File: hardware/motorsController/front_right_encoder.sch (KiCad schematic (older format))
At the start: 6 parts, among them Q1 Q_Photo_NPN

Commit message: add a pull-up to encoder's output
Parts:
- added R37: 1k, Resistor_SMD:R_0805_2012Metric, symbol Device:R_Small
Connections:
- net +3V3: now also R37.1
- net at Q1.1 (C), R29.2: now also R37.2
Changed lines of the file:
@@
 $Descr A4 11693 8268
 encoding utf-8
-Sheet 8 9
+Sheet 9 9
 Title ""
 Date ""
@@
 AR Path="/5FC04BEE/5FB0A7B2" Ref="D3"  Part="1"
 AR Path="/5FC04BF2/5FB0A7B2" Ref="D4"  Part="1"
-F 0 "D3" V 1739 2232 50  0000 R CNN
+F 0 "D4" V 1739 2232 50  0000 R CNN
 F 1 "LED" V 1648 2232 50  0000 R CNN
 F 2 "Connector_PinSocket_2.54mm:PinSocket_1x02_P2.54mm_Vertical" H 1700 2350 50  0001 C CNN
@@
 AR Path="/5FC04BEE/5FB0A7B8" Ref="Q3"  Part="1"
 AR Path="/5FC04BF2/5FB0A7B8" Ref="Q4"  Part="1"
-F 0 "Q3" H 2550 2300 50  0000 R CNN
+F 0 "Q4" H 2550 2300 50  0000 R CNN
 F 1 "Q_Photo_NPN" H 2950 2400 50  0000 R CNN
 F 2 "Connector_PinSocket_2.54mm:PinSocket_1x02_P2.54mm_Vertical" H 2450 2450 50  0001 C CNN
@@
 AR Path="/5FC04BEE/5FB0A7BE" Ref="#PWR0134"  Part="1"
 AR Path="/5FC04BF2/5FB0A7BE" Ref="#PWR0139"  Part="1"
-F 0 "#PWR0134" H 1700 2300 50  0001 C CNN
+F 0 "#PWR0139" H 1700 2300 50  0001 C CNN
 F 1 "GND" H 1705 2377 50  0000 C CNN
 F 2 "" H 1700 2550 50  0001 C CNN
@@
 AR Path="/5FC04BEE/5FB0A7C5" Ref="#PWR0135"  Part="1"
 AR Path="/5FC04BF2/5FB0A7C5" Ref="#PWR0140"  Part="1"
-F 0 "#PWR0135" H 1700 2000 50  0001 C CNN
+F 0 "#PWR0140" H 1700 2000 50  0001 C CNN
 F 1 "+3V3" H 1715 2323 50  0000 C CNN
 F 2 "" H 1700 2150 50  0001 C CNN
@@
 AR Path="/5FC04BEE/5FB0A7CC" Ref="#PWR0136"  Part="1"
 AR Path="/5FC04BF2/5FB0A7CC" Ref="#PWR0141"  Part="1"
-F 0 "#PWR0136" H 2350 2350 50  0001 C CNN
+F 0 "#PWR0141" H 2350 2350 50  0001 C CNN
 F 1 "GND" H 2355 2427 50  0000 C CNN
 F 2 "" H 2350 2600 50  0001 C CNN
@@
 AR Path="/5FC04BEE/5FB0A7D3" Ref="C9"  Part="1"
 AR Path="/5FC04BF2/5FB0A7D3" Ref="C11"  Part="1"
-F 0 "C9" H 3592 2296 50  0000 L CNN
+F 0 "C11" H 3592 2296 50  0000 L CNN
 F 1 "300pF" H 3592 2205 50  0000 L CNN
 F 2 "Capacitor_SMD:C_0805_2012Metric" H 3500 2250 50  0001 C CNN
@@
 AR Path="/5FC04BEE/5FB0A7D9" Ref="R33"  Part="1"
 AR Path="/5FC04BF2/5FB0A7D9" Ref="R35"  Part="1"
-F 0 "R33" V 3054 2100 50  0000 C CNN
+F 0 "R35" V 3054 2100 50  0000 C CNN
 F 1 "2M" V 3145 2100 50  0000 C CNN
 F 2 "Resistor_SMD:R_0805_2012Metric" H 3250 2100 50  0001 C CNN
@@
 AR Path="/5FC04BEE/5FB0B2E6" Ref="#PWR0137"  Part="1"
 AR Path="/5FC04BF2/5FB0B2E6" Ref="#PWR0142"  Part="1"
-F 0 "#PWR0137" H 3500 2150 50  0001 C CNN
+F 0 "#PWR0142" H 3500 2150 50  0001 C CNN
 F 1 "GND" H 3505 2227 50  0000 C CNN
 F 2 "" H 3500 2400 50  0001 C CNN
@@
 Wire Wire Line
 	2350 2150 2350 2100
-Wire Wire Line
-	2350 2100 3150 2100
 $Comp
 L Device:C_Small C6
@@
 AR Path="/5FC04BEE/5FB0F088" Ref="C10"  Part="1"
 AR Path="/5FC04BF2/5FB0F088" Ref="C12"  Part="1"
-F 0 "C10" V 3521 2100 50  0000 C CNN
+F 0 "C12" V 3521 2100 50  0000 C CNN
 F 1 "82nF" V 3612 2100 50  0000 C CNN
 F 2 "Capacitor_SMD:C_1206_3216Metric" H 3750 2100 50  0001 C CNN
@@
 AR Path="/5FC04BEE/5FB110C4" Ref="R34"  Part="1"
 AR Path="/5FC04BF2/5FB110C4" Ref="R36"  Part="1"
-F 0 "R34" H 4059 2296 50  0000 L CNN
+F 0 "R36" H 4059 2296 50  0000 L CNN
 F 1 "2M" H 4059 2205 50  0000 L CNN
 F 2 "Resistor_SMD:R_0805_2012Metric" H 4000 2250 50  0001 C CNN
@@
 AR Path="/5FC04BEE/5FB12EE4" Ref="#PWR0138"  Part="1"
 AR Path="/5FC04BF2/5FB12EE4" Ref="#PWR0143"  Part="1"
-F 0 "#PWR0138" H 4000 2150 50  0001 C CNN
+F 0 "#PWR0143" H 4000 2150 50  0001 C CNN
 F 1 "GND" H 4005 2227 50  0000 C CNN
 F 2 "" H 4000 2400 50  0001 C CNN
@@
 Wire Wire Line
 	4000 2400 4000 2350
+$Comp
+L power:+3.3V #PWR0144
+U 1 1 5FC0B227
+P 2950 1800
+AR Path="/5FB03879/5FC0B227" Ref="#PWR0144"  Part="1"
+AR Path="/5FBFC472/5FC0B227" Ref="#PWR0145"  Part="1"
+AR Path="/5FC04BEE/5FC0B227" Ref="#PWR0146"  Part="1"
+AR Path="/5FC04BF2/5FC0B227" Ref="#PWR0147"  Part="1"
+F 0 "#PWR0147" H 2950 1650 50  0001 C CNN
+F 1 "+3.3V" H 2965 1973 50  0000 C CNN
+F 2 "" H 2950 1800 50  0001 C CNN
+F 3 "" H 2950 1800 50  0001 C CNN
+	1    2950 1800
+	1    0    0    -1
+$EndComp
+$Comp
+L Device:R_Small R37
+U 1 1 5FC0D744
+P 2950 1950
+AR Path="/5FB03879/5FC0D744" Ref="R37"  Part="1"
+AR Path="/5FBFC472/5FC0D744" Ref="R38"  Part="1"
+AR Path="/5FC04BEE/5FC0D744" Ref="R39"  Part="1"
+AR Path="/5FC04BF2/5FC0D744" Ref="R40"  Part="1"
+F 0 "R40" H 3009 1996 50  0000 L CNN
+F 1 "1k" H 3009 1905 50  0000 L CNN
+F 2 "Resistor_SMD:R_0805_2012Metric" H 2950 1950 50  0001 C CNN
+F 3 "~" H 2950 1950 50  0001 C CNN
+	1    2950 1950
+	1    0    0    -1
+$EndComp
+Wire Wire Line
+	2950 1800 2950 1850
+Wire Wire Line
+	2950 2050 2950 2100
+Connection ~ 2950 2100
+Wire Wire Line
+	2950 2100 3150 2100
+Wire Wire Line
+	2350 2100 2950 2100
 $EndSCHEMATC

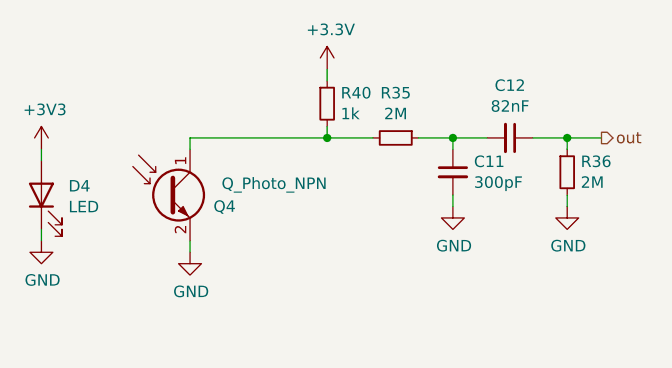
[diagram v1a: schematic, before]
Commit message: remove RC filter from collector and add resisor  before emiter
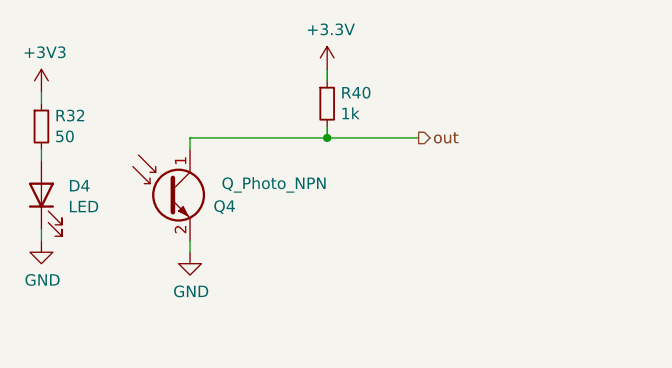
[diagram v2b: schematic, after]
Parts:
- removed C5: 300pF, Capacitor_SMD:C_0805_2012Metric, symbol Device:C_Small
- removed C6: 82nF, Capacitor_SMD:C_1206_3216Metric, symbol Device:C_Small
- removed R29, R30: 2M, Resistor_SMD:R_0805_2012Metric, symbol Device:R_Small
- added R31: 50, symbol Device:R_Small
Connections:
- net +3V3: now also R31.1; no longer D1.2 (A)
- net out: now also Q1.1 (C), R37.2
- new net: D1.2 (A), R31.2
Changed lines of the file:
@@
 $Descr A4 11693 8268
 encoding utf-8
-Sheet 9 9
+Sheet 8 9
 Title ""
 Date ""
@@
 L power:+3V3 #PWR0124
 U 1 1 5FB0A7C5
-P 1700 2150
+P 1700 1900
 AR Path="/5FB03879/5FB0A7C5" Ref="#PWR0124"  Part="1"
 AR Path="/5FBFC472/5FB0A7C5" Ref="#PWR0130"  Part="1"
 AR Path="/5FC04BEE/5FB0A7C5" Ref="#PWR0135"  Part="1"
 AR Path="/5FC04BF2/5FB0A7C5" Ref="#PWR0140"  Part="1"
-F 0 "#PWR0140" H 1700 2000 50  0001 C CNN
-F 1 "+3V3" H 1715 2323 50  0000 C CNN
-F 2 "" H 1700 2150 50  0001 C CNN
-F 3 "" H 1700 2150 50  0001 C CNN
-	1    1700 2150
+F 0 "#PWR0140" H 1700 1750 50  0001 C CNN
+F 1 "+3V3" H 1715 2073 50  0000 C CNN
+F 2 "" H 1700 1900 50  0001 C CNN
+F 3 "" H 1700 1900 50  0001 C CNN
+	1    1700 1900
 	1    0    0    -1
 $EndComp
@@
 Wire Wire Line
 	2350 2600 2350 2550
-$Comp
-L Device:C_Small C?
-U 1 1 5FB0A7D3
-P 3500 2250
-AR Path="/5FB0A7D3" Ref="C?"  Part="1"
-AR Path="/5FB03879/5FB0A7D3" Ref="C5"  Part="1"
-AR Path="/5FBFC472/5FB0A7D3" Ref="C7"  Part="1"
-AR Path="/5FC04BEE/5FB0A7D3" Ref="C9"  Part="1"
-AR Path="/5FC04BF2/5FB0A7D3" Ref="C11"  Part="1"
-F 0 "C11" H 3592 2296 50  0000 L CNN
-F 1 "300pF" H 3592 2205 50  0000 L CNN
-F 2 "Capacitor_SMD:C_0805_2012Metric" H 3500 2250 50  0001 C CNN
-F 3 "~" H 3500 2250 50  0001 C CNN
-	1    3500 2250
-	1    0    0    -1
-$EndComp
-$Comp
-L Device:R_Small R?
-U 1 1 5FB0A7D9
-P 3250 2100
-AR Path="/5FB0A7D9" Ref="R?"  Part="1"
-AR Path="/5FB03879/5FB0A7D9" Ref="R29"  Part="1"
-AR Path="/5FBFC472/5FB0A7D9" Ref="R31"  Part="1"
-AR Path="/5FC04BEE/5FB0A7D9" Ref="R33"  Part="1"
-AR Path="/5FC04BF2/5FB0A7D9" Ref="R35"  Part="1"
-F 0 "R35" V 3054 2100 50  0000 C CNN
-F 1 "2M" V 3145 2100 50  0000 C CNN
-F 2 "Resistor_SMD:R_0805_2012Metric" H 3250 2100 50  0001 C CNN
-F 3 "~" H 3250 2100 50  0001 C CNN
-	1    3250 2100
-	0    1    1    0
-$EndComp
-Wire Wire Line
-	3350 2100 3500 2100
-Wire Wire Line
-	3500 2100 3500 2150
-$Comp
-L power:GND #PWR0126
-U 1 1 5FB0B2E6
-P 3500 2400
-AR Path="/5FB03879/5FB0B2E6" Ref="#PWR0126"  Part="1"
-AR Path="/5FBFC472/5FB0B2E6" Ref="#PWR0132"  Part="1"
-AR Path="/5FC04BEE/5FB0B2E6" Ref="#PWR0137"  Part="1"
-AR Path="/5FC04BF2/5FB0B2E6" Ref="#PWR0142"  Part="1"
-F 0 "#PWR0142" H 3500 2150 50  0001 C CNN
-F 1 "GND" H 3505 2227 50  0000 C CNN
-F 2 "" H 3500 2400 50  0001 C CNN
-F 3 "" H 3500 2400 50  0001 C CNN
-	1    3500 2400
-	1    0    0    -1
-$EndComp
-Wire Wire Line
-	3500 2400 3500 2350
-Text HLabel 4150 2100 2    50   Output ~ 0
+Text HLabel 3350 2100 2    50   Output ~ 0
 out
 Wire Wire Line
 	2350 2150 2350 2100
-$Comp
-L Device:C_Small C6
-U 1 1 5FB0F088
-P 3750 2100
-AR Path="/5FB03879/5FB0F088" Ref="C6"  Part="1"
-AR Path="/5FBFC472/5FB0F088" Ref="C8"  Part="1"
-AR Path="/5FC04BEE/5FB0F088" Ref="C10"  Part="1"
-AR Path="/5FC04BF2/5FB0F088" Ref="C12"  Part="1"
-F 0 "C12" V 3521 2100 50  0000 C CNN
-F 1 "82nF" V 3612 2100 50  0000 C CNN
-F 2 "Capacitor_SMD:C_1206_3216Metric" H 3750 2100 50  0001 C CNN
-F 3 "~" H 3750 2100 50  0001 C CNN
-	1    3750 2100
-	0    1    1    0
-$EndComp
-Wire Wire Line
-	3650 2100 3500 2100
-Connection ~ 3500 2100
-$Comp
-L Device:R_Small R30
-U 1 1 5FB110C4
-P 4000 2250
-AR Path="/5FB03879/5FB110C4" Ref="R30"  Part="1"
-AR Path="/5FBFC472/5FB110C4" Ref="R32"  Part="1"
-AR Path="/5FC04BEE/5FB110C4" Ref="R34"  Part="1"
-AR Path="/5FC04BF2/5FB110C4" Ref="R36"  Part="1"
-F 0 "R36" H 4059 2296 50  0000 L CNN
-F 1 "2M" H 4059 2205 50  0000 L CNN
-F 2 "Resistor_SMD:R_0805_2012Metric" H 4000 2250 50  0001 C CNN
-F 3 "~" H 4000 2250 50  0001 C CNN
-	1    4000 2250
-	1    0    0    -1
-$EndComp
-Wire Wire Line
-	4000 2150 4000 2100
-Wire Wire Line
-	4000 2100 3850 2100
-Wire Wire Line
-	4150 2100 4000 2100
-Connection ~ 4000 2100
-$Comp
-L power:GND #PWR0127
-U 1 1 5FB12EE4
-P 4000 2400
-AR Path="/5FB03879/5FB12EE4" Ref="#PWR0127"  Part="1"
-AR Path="/5FBFC472/5FB12EE4" Ref="#PWR0133"  Part="1"
-AR Path="/5FC04BEE/5FB12EE4" Ref="#PWR0138"  Part="1"
-AR Path="/5FC04BF2/5FB12EE4" Ref="#PWR0143"  Part="1"
-F 0 "#PWR0143" H 4000 2150 50  0001 C CNN
-F 1 "GND" H 4005 2227 50  0000 C CNN
-F 2 "" H 4000 2400 50  0001 C CNN
-F 3 "" H 4000 2400 50  0001 C CNN
-	1    4000 2400
-	1    0    0    -1
-$EndComp
-Wire Wire Line
-	4000 2400 4000 2350
 $Comp
 L power:+3.3V #PWR0144
@@
 Connection ~ 2950 2100
 Wire Wire Line
-	2950 2100 3150 2100
+	2350 2100 2950 2100
 Wire Wire Line
-	2350 2100 2950 2100
+	2950 2100 3350 2100
+$Comp
+L Device:R_Small R31
+U 1 1 602F07E8
+P 1700 2050
+AR Path="/5FC04BEE/602F07E8" Ref="R31"  Part="1"
+AR Path="/5FBFC472/602F07E8" Ref="R30"  Part="1"
+AR Path="/5FB03879/602F07E8" Ref="R29"  Part="1"
+AR Path="/5FC04BF2/602F07E8" Ref="R32"  Part="1"
+F 0 "R32" H 1759 2096 50  0000 L CNN
+F 1 "50" H 1759 2005 50  0000 L CNN
+F 2 "" H 1700 2050 50  0001 C CNN
+F 3 "~" H 1700 2050 50  0001 C CNN
+	1    1700 2050
+	1    0    0    -1
+$EndComp
+Wire Wire Line
+	1700 1950 1700 1900
 $EndSCHEMATC

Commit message: layout a pcb for testing a motor driver
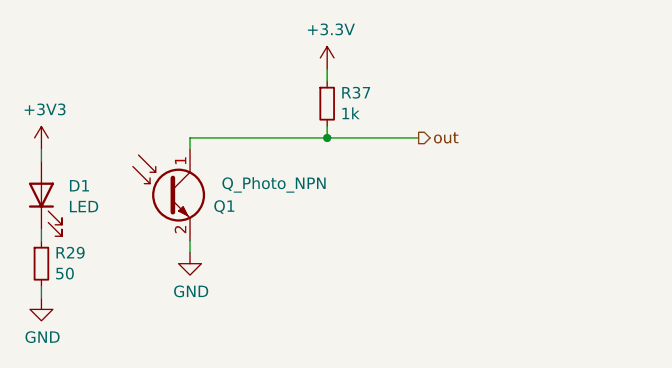
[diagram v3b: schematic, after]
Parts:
- R31: footprint (none) -> Resistor_SMD:R_0805_2012Metric
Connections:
- net +3V3: now also D1.2 (A); no longer R31.1
- net GND: now also R31.2; no longer D1.1 (K)
- new net: D1.1 (K), R31.1
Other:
- moved on the sheet: R29
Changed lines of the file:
@@
 $Descr A4 11693 8268
 encoding utf-8
-Sheet 8 9
+Sheet 6 9
 Title ""
 Date ""
@@
 AR Path="/5FC04BEE/5FB0A7B2" Ref="D3"  Part="1"
 AR Path="/5FC04BF2/5FB0A7B2" Ref="D4"  Part="1"
-F 0 "D4" V 1739 2232 50  0000 R CNN
+F 0 "D1" V 1739 2232 50  0000 R CNN
 F 1 "LED" V 1648 2232 50  0000 R CNN
 F 2 "Connector_PinSocket_2.54mm:PinSocket_1x02_P2.54mm_Vertical" H 1700 2350 50  0001 C CNN
@@
 AR Path="/5FC04BEE/5FB0A7B8" Ref="Q3"  Part="1"
 AR Path="/5FC04BF2/5FB0A7B8" Ref="Q4"  Part="1"
-F 0 "Q4" H 2550 2300 50  0000 R CNN
+F 0 "Q1" H 2550 2300 50  0000 R CNN
 F 1 "Q_Photo_NPN" H 2950 2400 50  0000 R CNN
 F 2 "Connector_PinSocket_2.54mm:PinSocket_1x02_P2.54mm_Vertical" H 2450 2450 50  0001 C CNN
@@
 L power:GND #PWR0123
 U 1 1 5FB0A7BE
-P 1700 2550
+P 1700 2800
 AR Path="/5FB03879/5FB0A7BE" Ref="#PWR0123"  Part="1"
 AR Path="/5FBFC472/5FB0A7BE" Ref="#PWR0129"  Part="1"
 AR Path="/5FC04BEE/5FB0A7BE" Ref="#PWR0134"  Part="1"
 AR Path="/5FC04BF2/5FB0A7BE" Ref="#PWR0139"  Part="1"
-F 0 "#PWR0139" H 1700 2300 50  0001 C CNN
-F 1 "GND" H 1705 2377 50  0000 C CNN
-F 2 "" H 1700 2550 50  0001 C CNN
-F 3 "" H 1700 2550 50  0001 C CNN
-	1    1700 2550
+F 0 "#PWR0123" H 1700 2550 50  0001 C CNN
+F 1 "GND" H 1705 2627 50  0000 C CNN
+F 2 "" H 1700 2800 50  0001 C CNN
+F 3 "" H 1700 2800 50  0001 C CNN
+	1    1700 2800
 	1    0    0    -1
 $EndComp
@@
 L power:+3V3 #PWR0124
 U 1 1 5FB0A7C5
-P 1700 1900
+P 1700 2150
 AR Path="/5FB03879/5FB0A7C5" Ref="#PWR0124"  Part="1"
 AR Path="/5FBFC472/5FB0A7C5" Ref="#PWR0130"  Part="1"
 AR Path="/5FC04BEE/5FB0A7C5" Ref="#PWR0135"  Part="1"
 AR Path="/5FC04BF2/5FB0A7C5" Ref="#PWR0140"  Part="1"
-F 0 "#PWR0140" H 1700 1750 50  0001 C CNN
-F 1 "+3V3" H 1715 2073 50  0000 C CNN
-F 2 "" H 1700 1900 50  0001 C CNN
-F 3 "" H 1700 1900 50  0001 C CNN
-	1    1700 1900
+F 0 "#PWR0124" H 1700 2000 50  0001 C CNN
+F 1 "+3V3" H 1715 2323 50  0000 C CNN
+F 2 "" H 1700 2150 50  0001 C CNN
+F 3 "" H 1700 2150 50  0001 C CNN
+	1    1700 2150
 	1    0    0    -1
 $EndComp
@@
 AR Path="/5FC04BEE/5FB0A7CC" Ref="#PWR0136"  Part="1"
 AR Path="/5FC04BF2/5FB0A7CC" Ref="#PWR0141"  Part="1"
-F 0 "#PWR0141" H 2350 2350 50  0001 C CNN
+F 0 "#PWR0125" H 2350 2350 50  0001 C CNN
 F 1 "GND" H 2355 2427 50  0000 C CNN
 F 2 "" H 2350 2600 50  0001 C CNN
@@
 AR Path="/5FC04BEE/5FC0B227" Ref="#PWR0146"  Part="1"
 AR Path="/5FC04BF2/5FC0B227" Ref="#PWR0147"  Part="1"
-F 0 "#PWR0147" H 2950 1650 50  0001 C CNN
+F 0 "#PWR0144" H 2950 1650 50  0001 C CNN
 F 1 "+3.3V" H 2965 1973 50  0000 C CNN
 F 2 "" H 2950 1800 50  0001 C CNN
@@
 AR Path="/5FC04BEE/5FC0D744" Ref="R39"  Part="1"
 AR Path="/5FC04BF2/5FC0D744" Ref="R40"  Part="1"
-F 0 "R40" H 3009 1996 50  0000 L CNN
+F 0 "R37" H 3009 1996 50  0000 L CNN
 F 1 "1k" H 3009 1905 50  0000 L CNN
 F 2 "Resistor_SMD:R_0805_2012Metric" H 2950 1950 50  0001 C CNN
@@
 L Device:R_Small R31
 U 1 1 602F07E8
-P 1700 2050
+P 1700 2650
 AR Path="/5FC04BEE/602F07E8" Ref="R31"  Part="1"
 AR Path="/5FBFC472/602F07E8" Ref="R30"  Part="1"
 AR Path="/5FB03879/602F07E8" Ref="R29"  Part="1"
 AR Path="/5FC04BF2/602F07E8" Ref="R32"  Part="1"
-F 0 "R32" H 1759 2096 50  0000 L CNN
-F 1 "50" H 1759 2005 50  0000 L CNN
-F 2 "" H 1700 2050 50  0001 C CNN
-F 3 "~" H 1700 2050 50  0001 C CNN
-	1    1700 2050
+F 0 "R29" H 1759 2696 50  0000 L CNN
+F 1 "50" H 1759 2605 50  0000 L CNN
+F 2 "Resistor_SMD:R_0805_2012Metric" H 1700 2650 50  0001 C CNN
+F 3 "~" H 1700 2650 50  0001 C CNN
+	1    1700 2650
 	1    0    0    -1
 $EndComp
 Wire Wire Line
-	1700 1950 1700 1900
+	1700 2750 1700 2800
 $EndSCHEMATC
